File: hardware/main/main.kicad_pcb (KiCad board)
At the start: 2 copper layers, 158 parts, among them J1 Conn_02x11_Odd_Even, J2 Conn_02x11_Odd_Even, J401 USART, J701 8P8C_Shielded, J702 8P8C_Shielded, J703 8P8C_Shielded, J704 8P8C_Shielded, K1 K100A, K802 SANYOU_SRD_Form_C, Q801 BCV27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

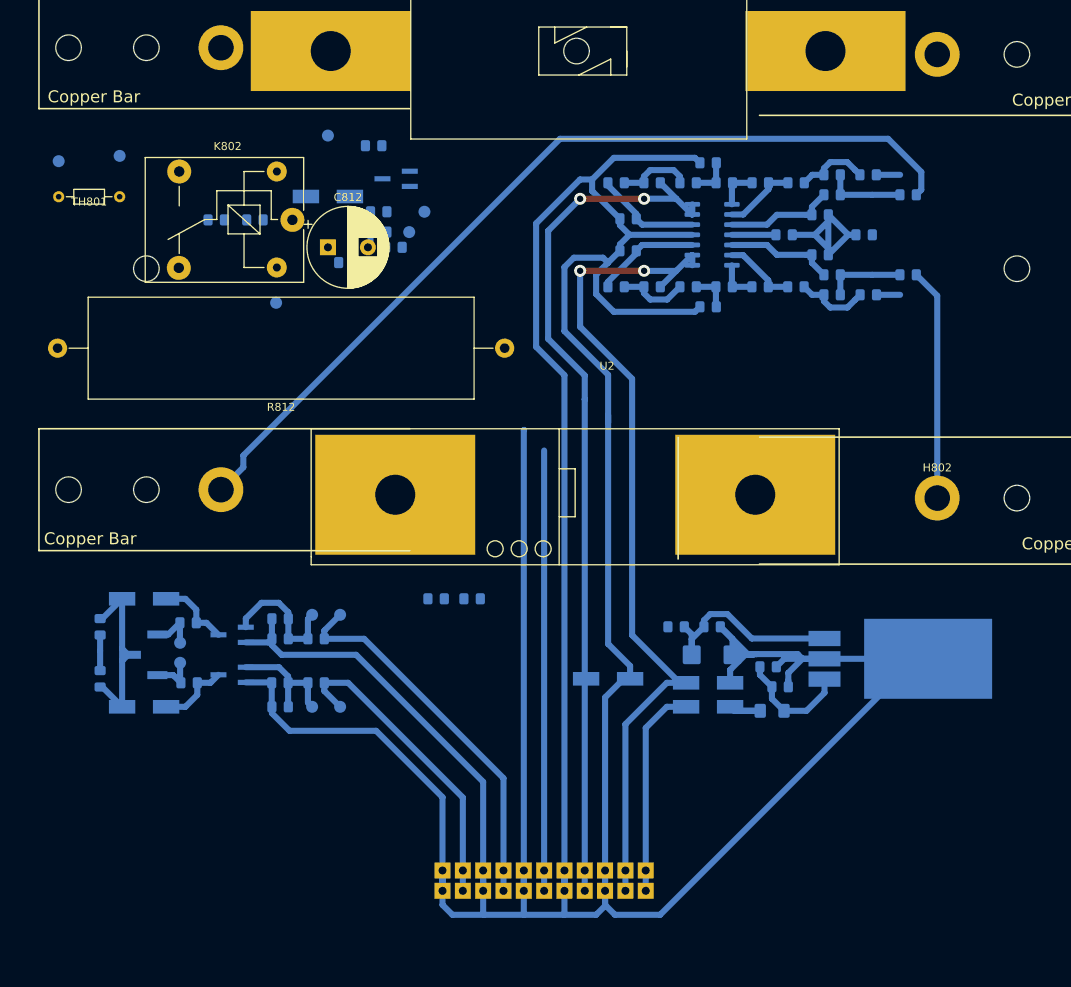
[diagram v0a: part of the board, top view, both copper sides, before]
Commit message: Signals tracks routed
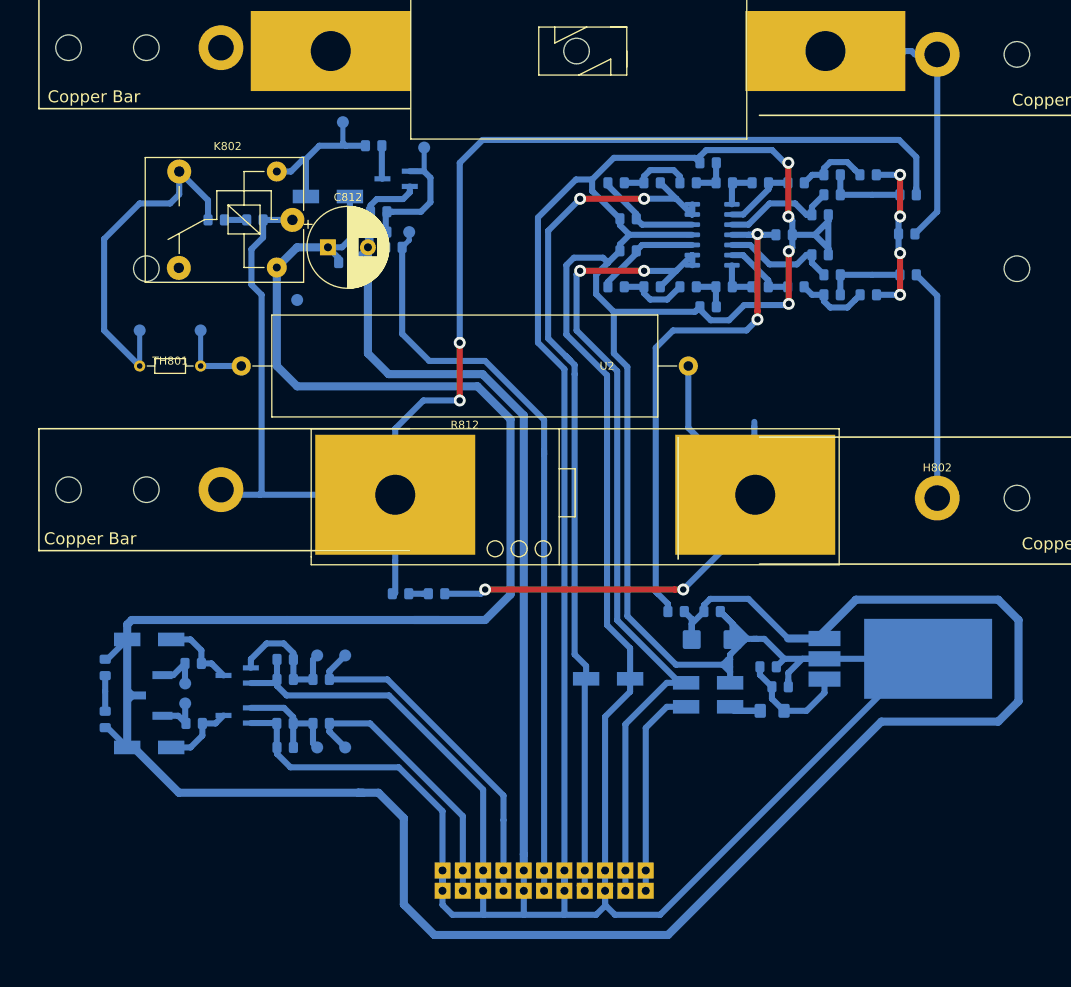
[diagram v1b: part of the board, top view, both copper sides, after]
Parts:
- moved TH801 27.6 mm to (75.6, -38.1), turned to 180 degrees
- moved TP811 27.6 mm to (75.6, -42.5)
- moved R812 23.1 mm to (136.5, -38.1)
- moved TP810 22.0 mm to (67.9, -42.5)
- moved TP803 8.03 mm to (103.5, -65.4)
- moved NT801 5.33 mm to (163.8, -54.6), turned to 0 degrees
- moved C801 5.12 mm to (86.1, 9.58)
- moved C809 5.12 mm to (86.1, 1.08)
- moved D802 5.12 mm to (69.1, 9.58)
- moved D804 5.12 mm to (69.1, -3.92)
- moved K1 5.12 mm to (69.1, 3.08)
- moved Q801 5.12 mm to (80.1, 5.58)
- moved Q803 5.12 mm to (80.1, 0.58)
- moved R801 5.12 mm to (90.6, 6.58)
- moved R803 5.12 mm to (86.1, 6.58)
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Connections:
- K802 pad 4: (no net) -> Net-(K802-Pad4)
- U1 pad : (no net) -> GNDPWR
- U201 pad 5: (no net) -> Net-(U201-Pad5)
- U202 pad 10: (no net) -> Net-(U202-Pad10)
- U202 pad 11: (no net) -> Net-(U202-Pad11)
- U202 pad 3: (no net) -> Net-(U202-Pad3)
- U202 pad 4: (no net) -> Net-(U202-Pad4)
- U202 pad 5: (no net) -> Net-(U202-Pad5)
- U202 pad 6: (no net) -> Net-(U202-Pad6)
- U401 pad 13: (no net) -> Net-(U401-Pad13)
- U401 pad 16: (no net) -> Net-(U401-Pad16)
- U401 pad 28: (no net) -> Net-(U401-Pad28)
- U401 pad 4: (no net) -> Net-(U401-Pad4)
- U401 pad 5: (no net) -> Net-(U401-Pad5)
- U401 pad 6: (no net) -> Net-(U401-Pad6)
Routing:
- net /CHARGER/+12V: track 49.0 -> 384.6 mm
- net GNDPWR: track 584.5 -> 751.5 mm, vias 0 -> 4
- net /CHARGER/+CAP: track 37.2 -> 111.3 mm, vias 0 -> 2
- net /CHARGER/U_BAT+: track 111.4 -> 185.3 mm, vias 0 -> 2
- net +12VA: track 5.50 -> 65.5 mm, vias 0 -> 2
- net /CHARGER/CH: track 0.00 -> 44.3 mm
- net /CHARGER/Charge: track 55.0 -> 94.6 mm
- net Net-(U401-Pad4): track 0.00 -> 23.3 mm
- net (no net): track 23.3 -> 0.00 mm
- net Net-(D803-Pad2): track 0.00 -> 20.2 mm
- net Net-(C802-Pad1): track 0.00 -> 19.4 mm
- net GNDA: track 5.92 -> 21.2 mm, vias 0 -> 4
- net Net-(R812-Pad2): track 0.00 -> 9.52 mm
- net /CHARGER/S_RL_ON: track 0.00 -> 4.17 mm
- net /CHARGER/RL_ON: track 38.7 -> 34.6 mm
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
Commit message: First version PCB
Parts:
- added LOGO1: Zenite, KicadZeniteSolarLibrary18:zenite, F.Cu at (163.2, 24.1)
- added LOGO2: Logo_Open_Hardware_Small, Symbol:OSHW-Logo2_9.8x8mm_Copper, B.Cu at (179.1, 29.8)
- moved R814 214.2 mm to (168.3, -49.5)
- moved D806 214.0 mm to (168.3, -52.1)
- moved D805 208.8 mm to (168.3, -57.1)
- moved R813 208.5 mm to (168.3, -59.5)
- moved H301 197.9 mm to (113.0, -49.5)
- moved D807 161.5 mm to (95.2, -63.5), turned to 180 degrees
- moved R815 158.2 mm to (93.3, -61.6)
- moved D808 147.8 mm to (93.9, -45.7)
- moved R816 147.7 mm to (93.8, -48.3)
- moved J703 29.9 mm to (143.9, 103.2)
- moved J704 29.9 mm to (162.9, 103.2)
- moved C808 12.1 mm to (74.7, 4.45), turned to 0 degrees
- moved C804 11.8 mm to (74.7, 1.91), turned to 180 degrees
- moved H806 9.75 mm to (59.1, -49.5)
- moved H3 9.75 mm to (187.3, -49.5)
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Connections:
- U1 pad : GNDPWR -> (no net)
- U501 pad : (no net) -> GND
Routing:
- net GND: track 108.8 -> 248.7 mm
- net /CONTROLLER/+18V_OUT: track 62.4 -> 194.7 mm
- net /CONTROLLER/sheet5CA5A59C/CAN_H: track 50.6 -> 101.8 mm
- net /CONTROLLER/RL_ON: track 0.00 -> 37.6 mm
- net /CONTROLLER/RL_OFF: track 0.00 -> 35.9 mm
- net /CONTROLLER/Charge: track 0.00 -> 33.2 mm
- net /CONTROLLER/sig_bat+: track 0.00 -> 31.1 mm
- net /CONTROLLER/sig_cap+: track 0.00 -> 28.9 mm
- net /CONTROLLER/sheet5CA5A59C/CAN_L: track 48.2 -> 75.0 mm, vias 2 -> 4
- net Net-(U401-Pad4): track 23.3 -> 0.00 mm
- net /CHARGER/+CAP: track 111.3 -> 127.6 mm
- net GNDPWR: track 751.5 -> 765.1 mm
- net /CHARGER/+12V: track 384.6 -> 394.3 mm
- net /CHARGER/CH: track 44.3 -> 38.3 mm
- net /CHARGER/S_RL_ON: track 4.17 -> 7.01 mm
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- added copper zone on B.Cu, net /CHARGER/+CAP
- added copper zone on B.Cu, net /CHARGER/U_BAT+
- added copper zone on B.Cu, net /CHARGER/U_BAT-
- added copper zone on B.Cu, net GNDPWR

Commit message: Small updates
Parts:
- moved C802 0.48 mm to (97.8, -56.9)
- moved C808 0.38 mm to (74.7, 4.06)
- moved C804 0.38 mm to (74.7, 1.52)
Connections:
- U1 pad : (no net) -> GNDPWR
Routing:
- net /CONTROLLER/sheet5CA5A59C/CAN_L: track 75.0 -> 86.9 mm, vias 4 -> 6
- net /CONTROLLER/sheet5CA5A59C/CAN_H: track 101.8 -> 103.0 mm

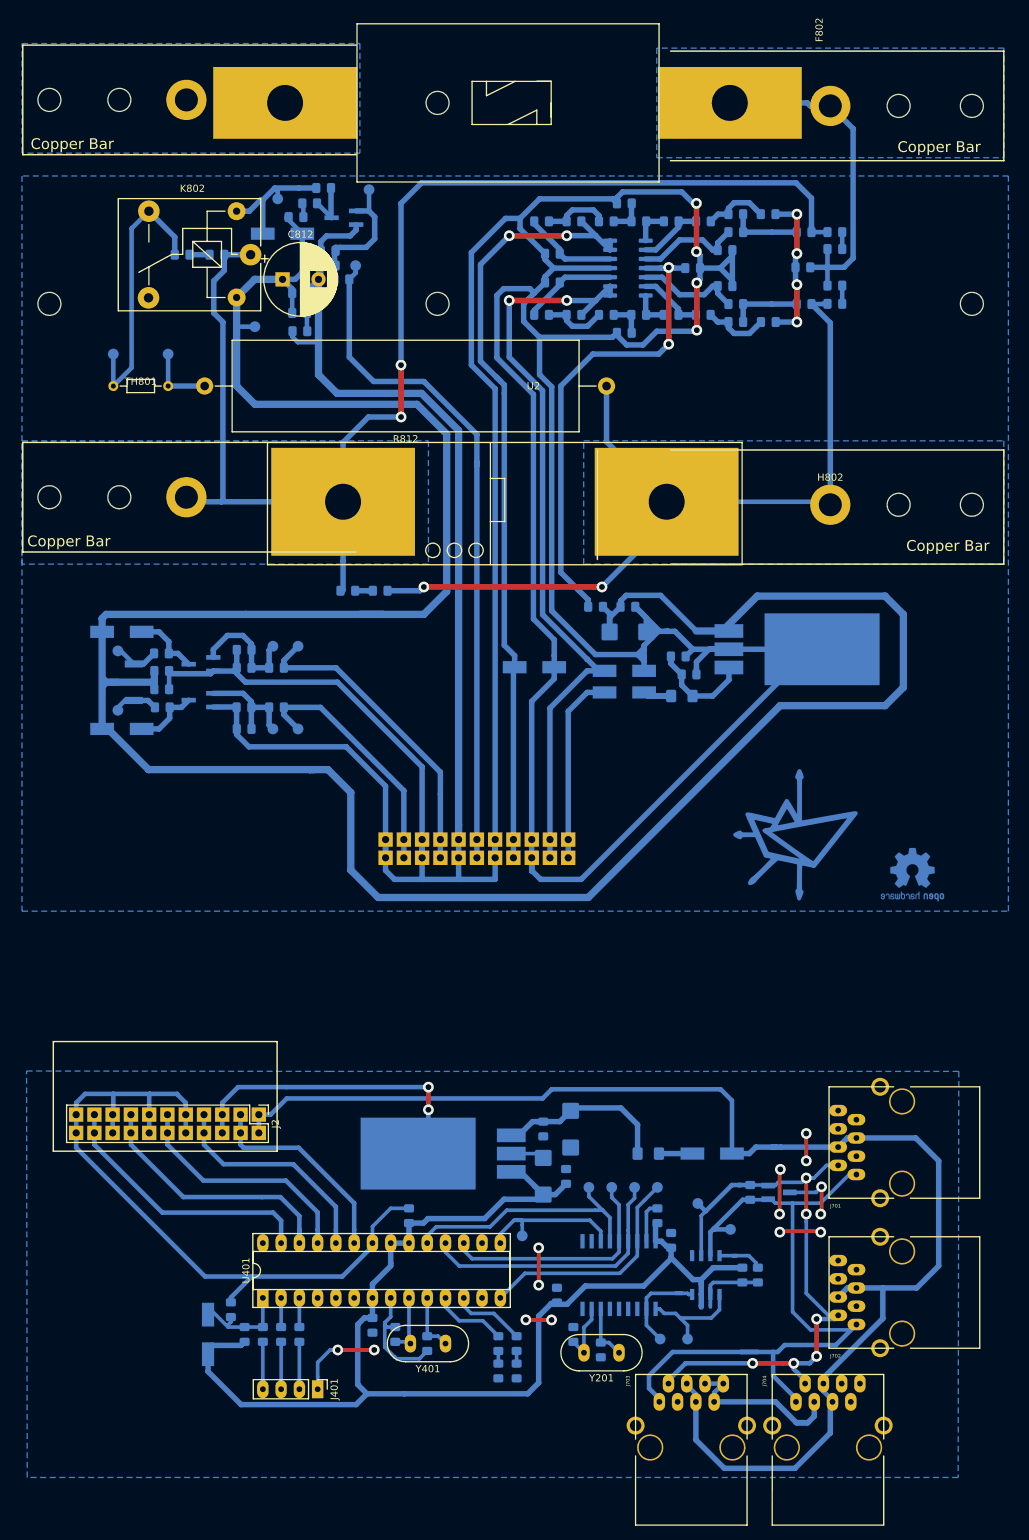
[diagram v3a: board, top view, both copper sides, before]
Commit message: Connector to join the modules, were centrailized Compacted Atmega PCB
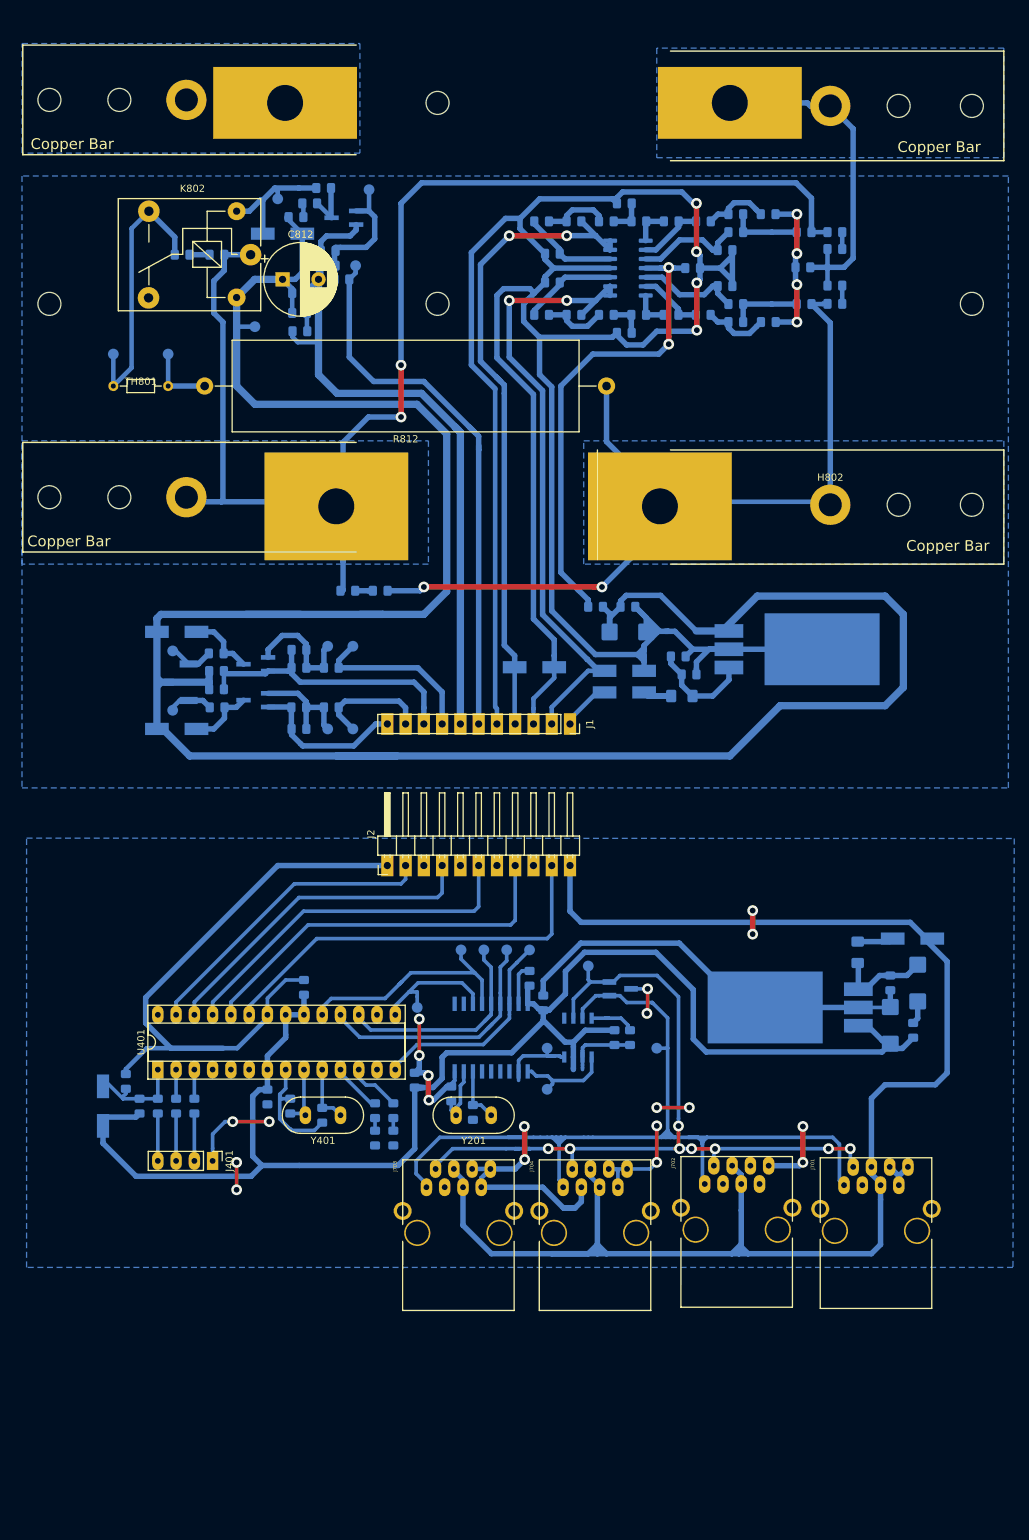
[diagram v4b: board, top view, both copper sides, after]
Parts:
- removed LOGO1: Zenite, KicadZeniteSolarLibrary18:zenite
- removed LOGO2: Logo_Open_Hardware_Small, Symbol:OSHW-Logo2_9.8x8mm_Copper
- removed R201: 120, Resistor_SMD:R_0805_2012Metric_Pad1.15x1.40mm_HandSolder
- F802, U2: moved to B.Cu
- J1: value Conn_02x11_Odd_Even -> Conn_01x11; footprint KicadZeniteSolarLibrary18:PinHeader_2x11_P2.54mm_Vertical_HandSoldering -> Connector_PinSocket_2.54mm:PinSocket_1x11_P2.54mm_Vertical; moved to F.Cu
- J2: value Conn_02x11_Odd_Even -> Conn_01x11; footprint KicadZeniteSolarLibrary18:PinHeader_2x11_P2.54mm_Vertical_HandSoldering -> Connector_PinHeader_2.54mm:PinHeader_1x11_P2.54mm_Horizontal
- moved C504 52.6 mm to (176.0, 50.8)
- moved C502 52.4 mm to (176.0, 44.9)
- moved U501 52.4 mm to (170.3, 45.8)
- moved C503 52.4 mm to (179.2, 51.5)
- moved C501 52.4 mm to (179.8, 44.9)
- moved J704 44.0 mm to (130.5, 73.3)
- moved J703 44.0 mm to (111.5, 73.3)
- moved TP204 43.4 mm to (128.3, 54.0)
- moved D501 40.9 mm to (179.1, 38.7)
- moved F501 40.4 mm to (171.4, 40.6), turned to 270 degrees
- moved TP203 39.8 mm to (128.3, 59.7)
- moved J2 39.0 mm to (106.0, 28.6), turned to 90 degrees
- moved C204 37.5 mm to (114.9, 60.3)
- moved C203 37.5 mm to (117.9, 62.9)
- moved C205 37.5 mm to (137.6, 52.5)
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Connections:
- J1 pad 10: GNDPWR -> /CHARGER/RL_ON
- J1 pad 11: /CHARGER/Charge -> GNDPWR
- J1 pad 2: /CHARGER/+18V_IN -> /CHARGER/sig_cap+
- J1 pad 3: /CHARGER/sig_cap+ -> GNDPWR
- J1 pad 4: /CHARGER/sig_cap+ -> /CHARGER/sig_bat+
- J1 pad 6: GNDPWR -> /CHARGER/Charge
- J1 pad 7: /CHARGER/sig_bat+ -> GNDPWR
- J1 pad 8: /CHARGER/sig_bat+ -> /CHARGER/RL_OFF
- J2 pad 1: /CONTROLLER/+18V_OUT -> GND
- J2 pad 10: GND -> /CONTROLLER/sig_cap+
- J2 pad 11: /CONTROLLER/Charge -> /CONTROLLER/+18V_OUT
- J2 pad 2: /CONTROLLER/+18V_OUT -> /CONTROLLER/RL_ON
- J2 pad 3: /CONTROLLER/sig_cap+ -> GND
- J2 pad 4: /CONTROLLER/sig_cap+ -> /CONTROLLER/RL_OFF
- J2 pad 6: GND -> /CONTROLLER/Charge
- J2 pad 7: /CONTROLLER/sig_bat+ -> GND
- U1 pad : GNDPWR -> (no net)
- U2 pad 4: /CHARGER/U_BAT+ -> /CHARGER/+CAP
- U2 pad 5: /CHARGER/+CAP -> /CHARGER/U_BAT+
- U501 pad : GND -> (no net)
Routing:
- net GNDPWR: track 765.1 -> 580.3 mm
- net GND: track 248.9 -> 295.5 mm, vias 16 -> 20
- net +5V: track 170.6 -> 213.7 mm
- net /CONTROLLER/sig_cap+: track 28.9 -> 56.9 mm
- net /CONTROLLER/sheet5CA5A59C/CAN_H: track 103.0 -> 130.5 mm
- net /CONTROLLER/sheet5CA5A59C/CAN_L: track 86.9 -> 113.3 mm, vias 6 -> 8
- net /CONTROLLER/+18V_OUT: track 194.7 -> 218.1 mm
- net /CONTROLLER/sig_bat+: track 31.1 -> 53.6 mm
- net /CHARGER/+12V: track 394.3 -> 373.6 mm
- net /CHARGER/+18V_IN: track 26.5 -> 7.00 mm
- net /CHARGER/RL_OFF: track 43.5 -> 24.0 mm
- net /CHARGER/sig_bat+: track 111.2 -> 91.9 mm
- net /CHARGER/sig_cap+: track 106.9 -> 88.2 mm
- net /CHARGER/RL_ON: track 34.6 -> 16.1 mm
- net /CHARGER/Charge: track 94.6 -> 77.2 mm
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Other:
- net class Default: trace_width 0.762 -> 0.508

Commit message: 3D fixation
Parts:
- J1: footprint Connector_PinSocket_2.54mm:PinSocket_1x11_P2.54mm_Vertical -> Connector_PinSocket_2.54mm:PinSocket_1x11_P2.54mm_Horizontal; moved to B.Cu
- J2: moved to B.Cu
- J401: footprint Connector_PinHeader_2.54mm:PinHeader_1x04_P2.54mm_Vertical -> Connector_PinHeader_2.54mm:PinHeader_1x04_P2.54mm_Vertical_SMD_Pin1Left; moved to B.Cu
- moved J2 25.4 mm to (131.4, 28.6)
- moved J401 4.33 mm to (78.1, 67.3), turned to 90 degrees
- turned J1 to 90 degrees
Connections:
- J2 pad 1: GND -> /CONTROLLER/+18V_OUT
- J2 pad 10: /CONTROLLER/sig_cap+ -> /CONTROLLER/RL_ON
- J2 pad 11: /CONTROLLER/+18V_OUT -> GND
- J2 pad 2: /CONTROLLER/RL_ON -> /CONTROLLER/sig_cap+
- J2 pad 4: /CONTROLLER/RL_OFF -> /CONTROLLER/sig_bat+
- J2 pad 8: /CONTROLLER/sig_bat+ -> /CONTROLLER/RL_OFF
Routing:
- net Net-(J401-Pad2): track 6.59 -> 2.67 mm
- net Net-(C405-Pad2): track 6.59 -> 2.67 mm
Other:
- board outline added: 137.8 x 170.2 mm
